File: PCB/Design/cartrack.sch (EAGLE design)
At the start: 1 part

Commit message: Done most of the GSM schematic.
Power and GPS remain
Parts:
- added C1: 1uF, resistor:C-EUC0603
- added LED1: (no value), led:LEDSML0603
- added Q1, Q2: (no value), semicon-smd-ipc:NPN-TRANSISTOR_SOT23W
- added R1, R2, R3: 22R, resistor:R-EU_R0603
- added R4, R5, R6, R7: 4k7, resistor:R-EU_R0603
- added R8: 300, resistor:R-EU_R0603
- added U$3: SIMHOLDER, SparkFun-Connectors:SIMHOLDER
- added U$4: SMF05C, Simplex-DiscreteSemi:SMF05C
- added U1: ATMEGA644P-20AU, Atmel_By_element14_Batch_1:ATMEGA644P-20AU
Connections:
- new net +2V8: U$1.VDD_EXT, U1.AVCC, U1.VCC, U1.VCC_2, U1.VCC_3
- new net +4V: LED1.A, U$1.VBAT1, U$1.VBAT2, U$1.VBAT3
- new net 0V: C1.2, R5.1, R7.1, U$1.AGND, U$1.GND1, U$1.GND2, U$1.GND3, U$1.GND4, U$1.GND5, U$1.GND6, U$1.GND7, U$1.GND8, U$3.C5, U$4.ANODE, U1.GND, U1.GND_2, U1.GND_3, U1.GND_4
- new net GSM_PWR: Q1.C, U$1.PWRKEY
- new net GSM_RX: U$1.RXD, U1.PD3
- new net GSM_STATUS: U$1.STATUS, U1.PD5
- new net GSM_TX: U$1.TXD, U1.PD2
- new net N$1: R1.1, U$3.C7, U$4.CATODE1
- new net N$10: LED1.C, R8.2
- new net N$2: R2.2, U$3.C3, U$4.CATODE5
- new net N$3: R3.2, U$3.C2, U$4.CATODE3
- new net N$4: Q1.E, R5.2
- new net N$5: Q1.B, R4.2
- new net N$6: R4.1, U1.PD4
- new net N$7: Q2.E, R7.2
- new net N$8: Q2.B, R6.2
- new net N$9: Q2.C, R8.1
- new net NETLIGHT: R6.1, U$1.NETLIGHT
- new net SIM_CLK: R2.1, U$1.SIM_CLK
- new net SIM_DATA: R1.2, U$1.SIM_DATA
- new net SIM_RST: R3.1, U$1.SIM_RST
- new net SIM_VDD: C1.1, U$1.SIM_VDD, U$3.C1, U$4.CATODE2

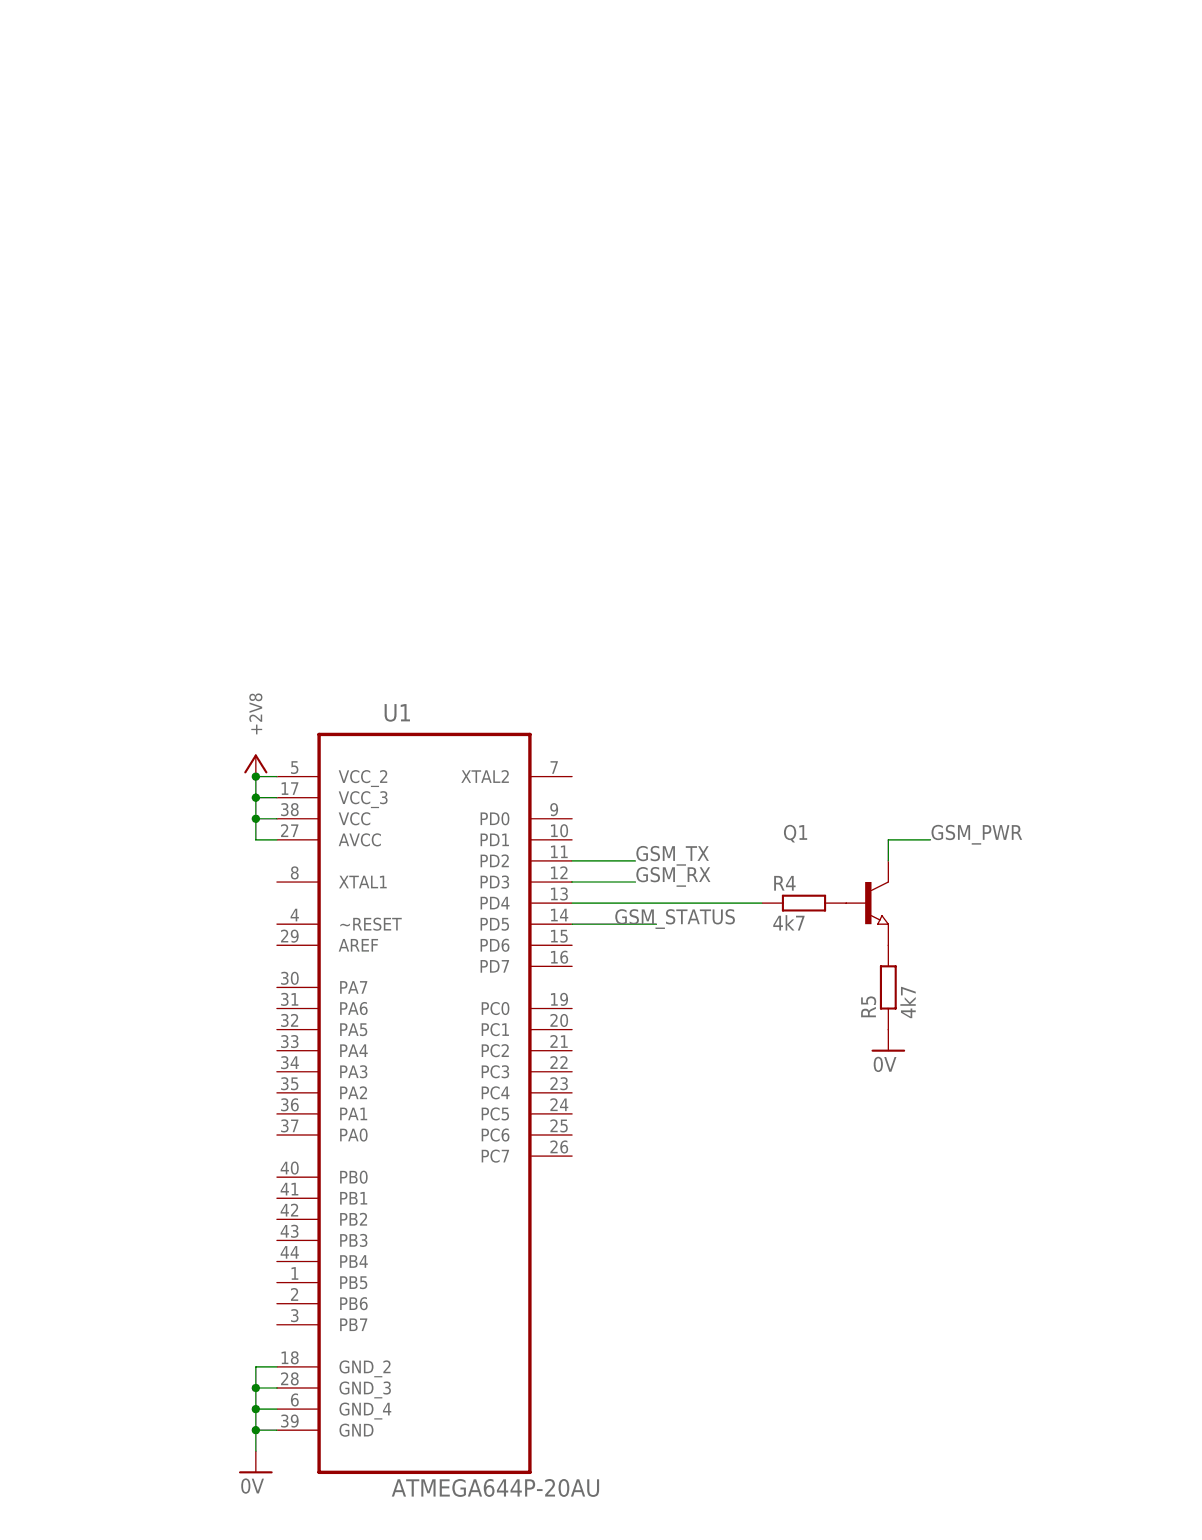
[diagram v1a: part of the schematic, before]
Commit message: Added GPS to schematic. Need to do power
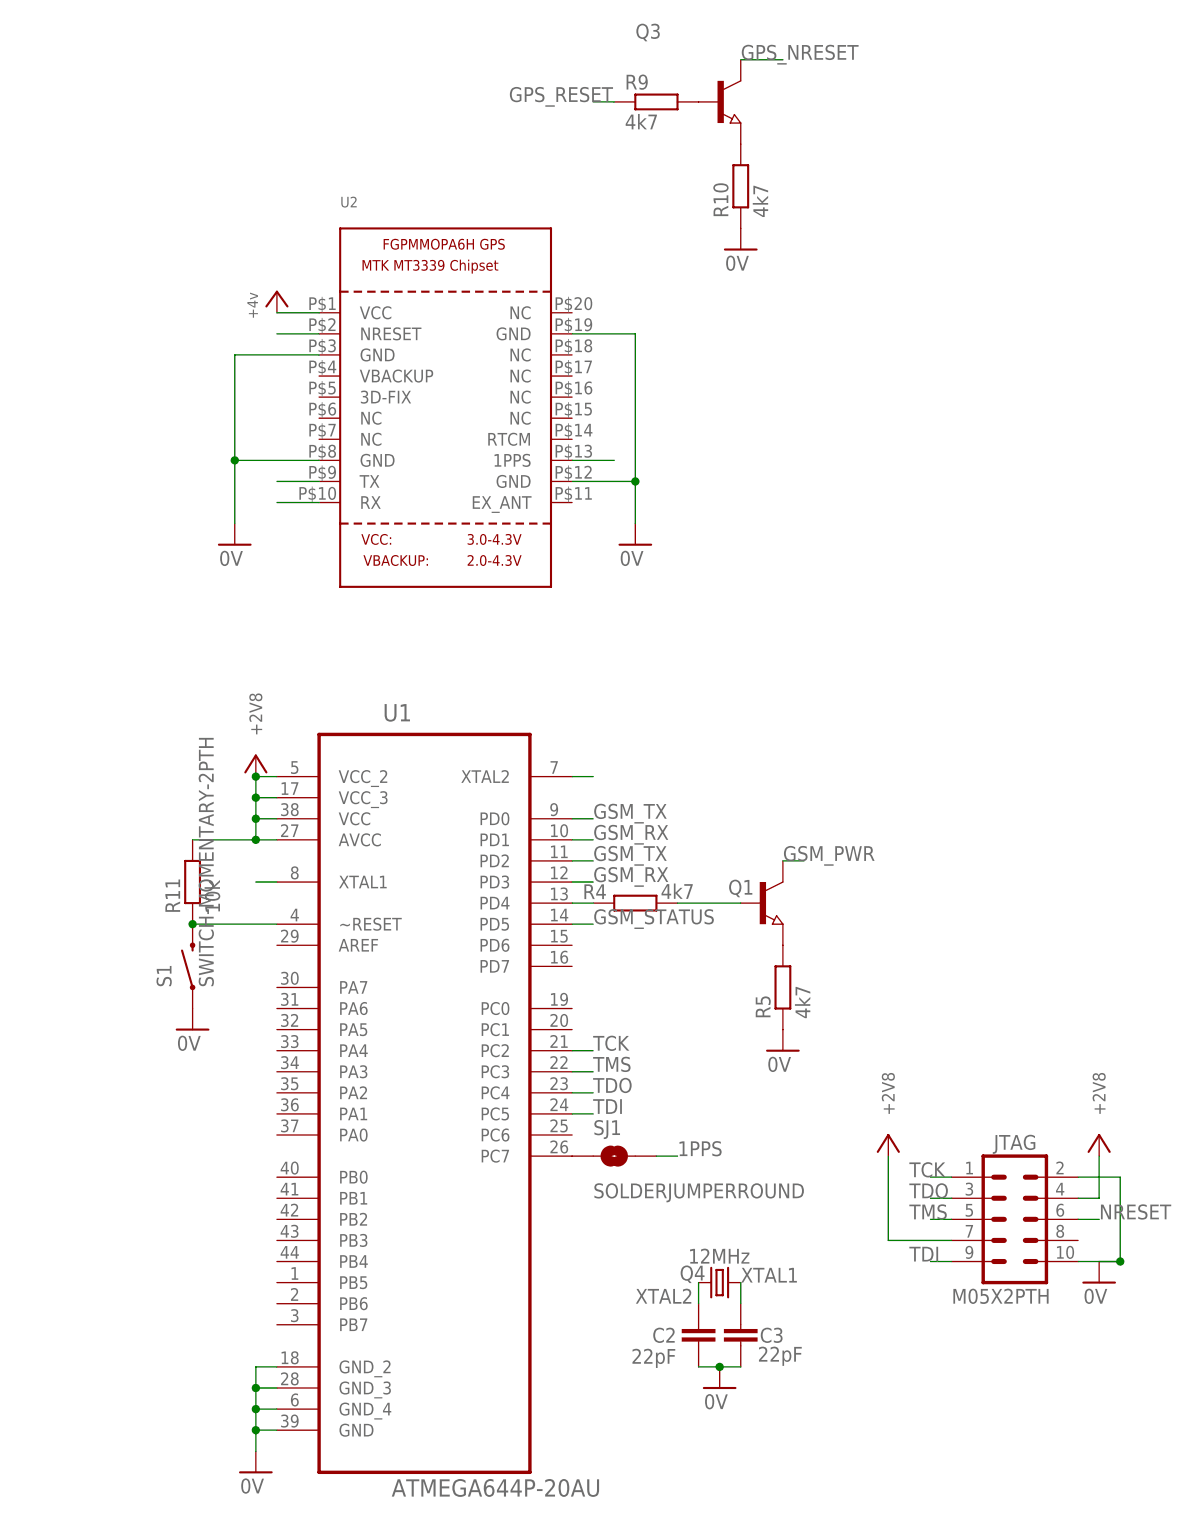
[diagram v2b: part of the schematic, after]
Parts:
- added C2, C3: 22pF, SparkFun-Passives:CAP0603-CAP
- added JTAG: M05X2PTH, SparkFun-Connectors:M05X2PTH
- added Q3: (no value), semicon-smd-ipc:NPN-TRANSISTOR_SOT23W
- added Q4: 12MHz, crystal:CRYSTALSM49
- added R10, R9: 4k7, resistor:R-EU_R0603
- added R11: 10k, resistor:R-EU_R0603
- added S1: SWITCH-MOMENTARY-2PTH, SparkFun-Electromechanical:SWITCH-MOMENTARY-2PTH
- added SJ1: SOLDERJUMPERROUND, SparkFun-Retired:SOLDERJUMPERROUND
- added U2: (no value), adafruit:GPS_FGPMMOPA6H
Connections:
- new net 1PPS: SJ1.2, U2.1PPS
- new net GPS_NRESET: Q3.C, U2.NRESET
- new net GPS_RESET: R9.1
- new net GPS_RX: U2.RX
- new net GPS_TX: U2.TX
- new net N$11: Q3.B, R9.2
- new net N$12: Q3.E, R10.2
- new net N$13: SJ1.1, U1.PC7
- new net NRESET: JTAG.6, R11.1, S1.2, U1.~RESET
- new net TCK: JTAG.1, U1.PC2
- new net TDI: JTAG.9, U1.PC5
- new net TDO: JTAG.3, U1.PC4
- new net TMS: JTAG.5, U1.PC3
- new net XTAL1: C3.1, Q4.2, U1.XTAL1
- new net XTAL2: C2.1, Q4.1, U1.XTAL2
- net +2V8: now also JTAG.4, JTAG.7, R11.2
- net +4V: now also U2.VCC
- net 0V: now also C2.2, C3.2, JTAG.10, JTAG.2, R10.1, S1.1, U2.GND@1, U2.GND@2, U2.GND@3, U2.GND@4
- net GSM_RX: now also U1.PD1
- net GSM_TX: now also U1.PD0
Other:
- moved on the sheet: Q1, R4, R5

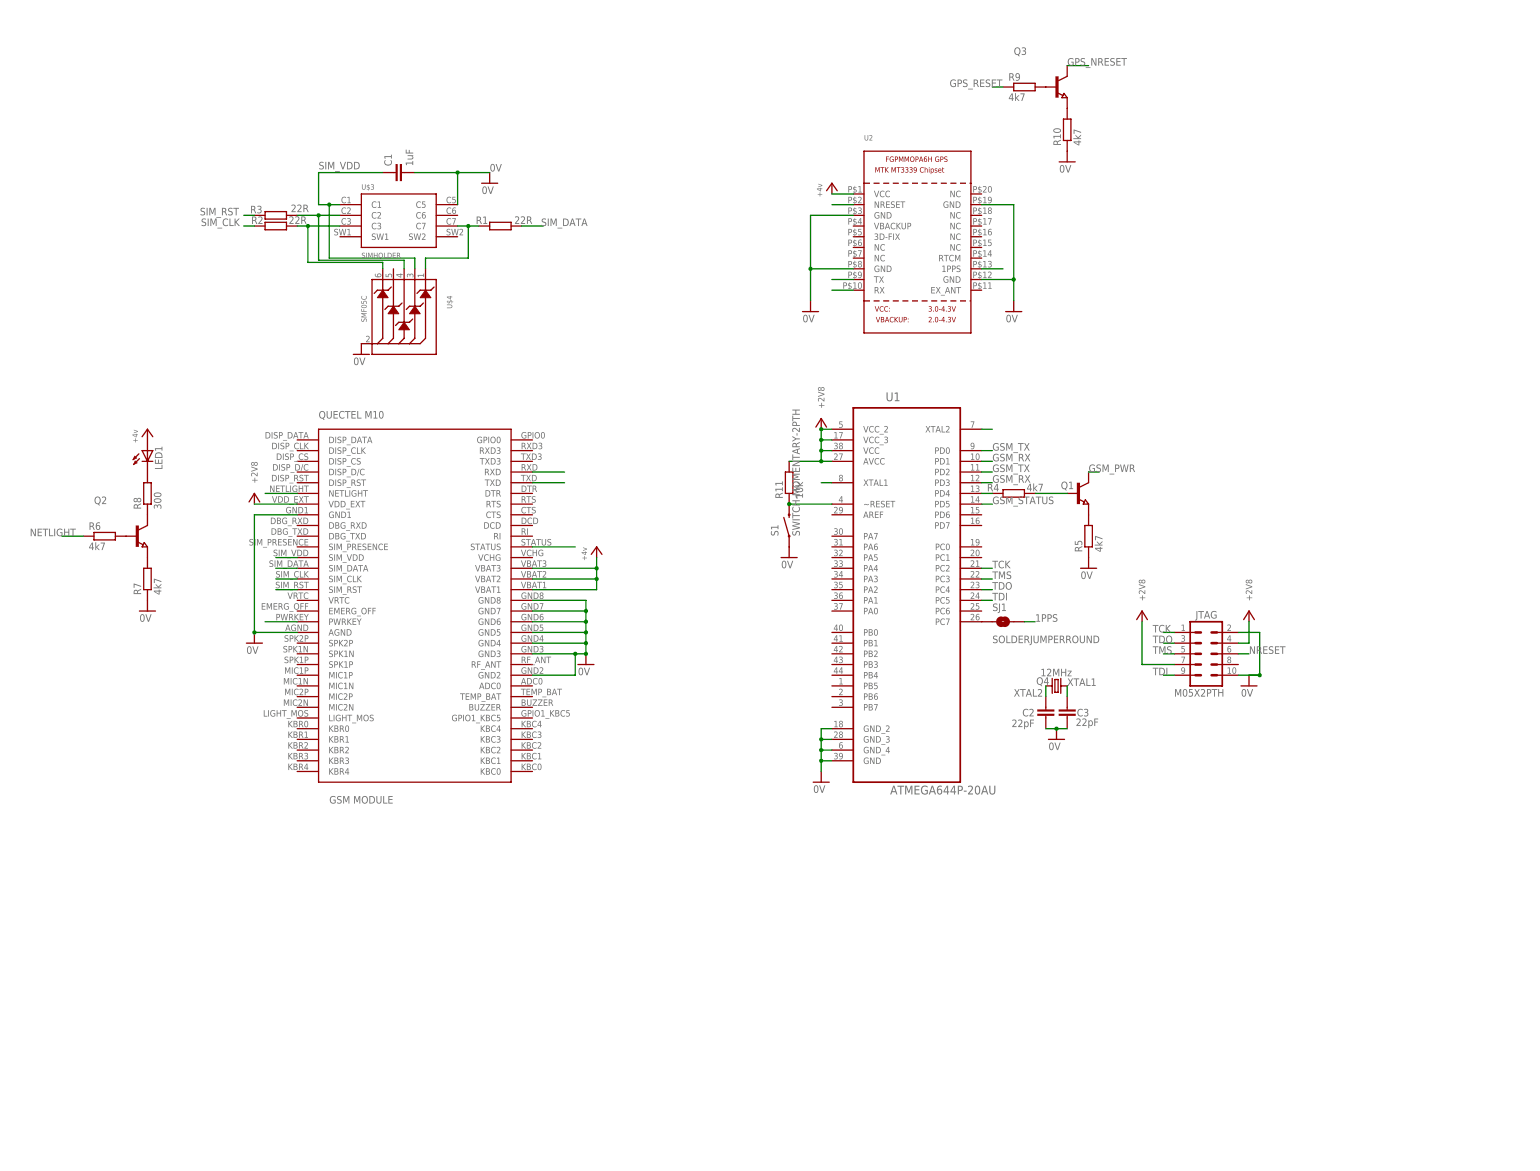
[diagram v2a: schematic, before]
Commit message: Added all major components to schematic.
Need to do the antenna, decoupling capacitors and layout
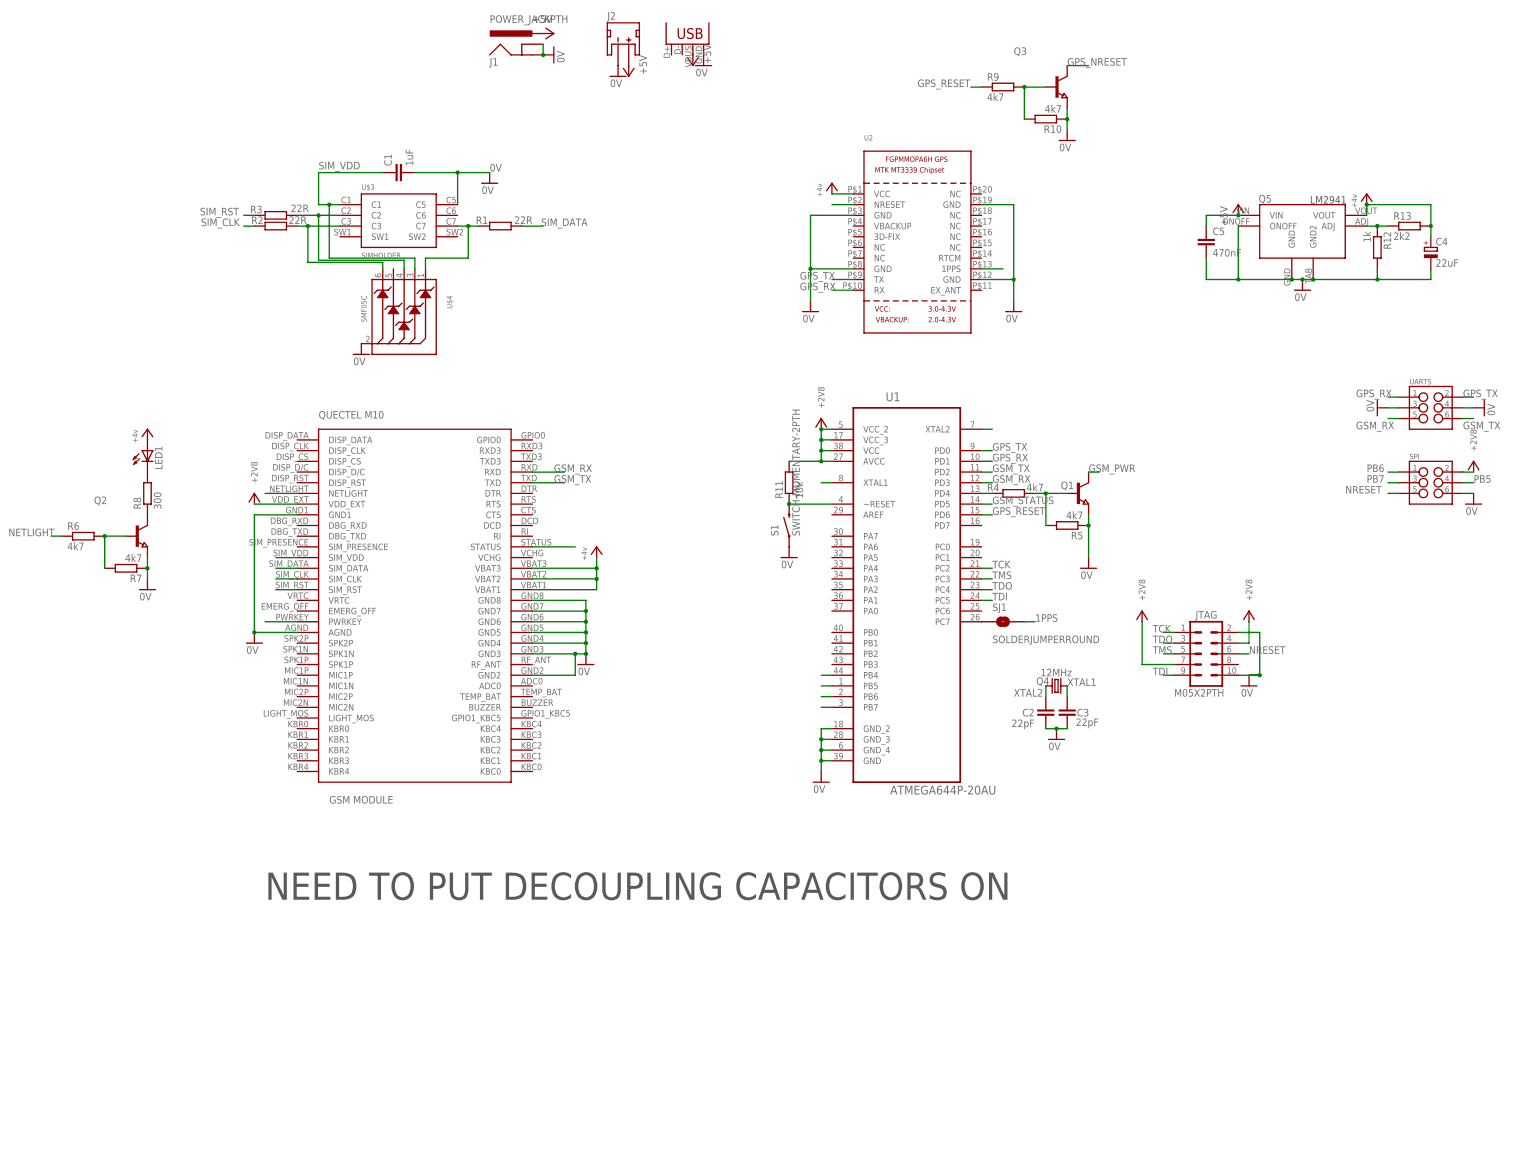
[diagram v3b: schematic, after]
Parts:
- added C4: 22uF, resistor:CPOL-EUE3.5-8
- added C5: 470nF, resistor:C-EU025-024X044
- added J1: POWER_JACKPTH, SparkFun-Connectors:POWER_JACKPTH
- added J2: (no value), SparkFun-Connectors:JST_2MM_MALE
- added JP1: USBSMD, SparkFun-Connectors:USBSMD
- added Q5: LM2941, misc:LM2941
- added R12: 1k, resistor:R-EU_R0603
- added R13: 2k2, resistor:R-EU_R0603
- added SPI, UARTS: (no value), SparkFun-Connectors:M03X2NO_SILK
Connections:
- removed net N$12: Q3.E, R10.2
- removed net N$4: Q1.E, R5.2
- new net +5V: C5.1, J1.PWR, J2.+, JP1.VBUS, Q5.VIN
- new net PB4: U1.PB4
- new net PB5: SPI.4, U1.PB5
- new net PB6: SPI.1, U1.PB6
- new net PB7: SPI.3, U1.PB7
- net +2V8: now also SPI.2
- net +4V: now also C4.+, Q5.VOUT, R13.2
- net 0V: now also C4.-, C5.2, J1.GND, J1.GNDBREAK, J2.-, JP1.GND, Q1.E, Q2.E, Q3.E, Q5.GND, Q5.GND2, Q5.ONOFF, R12.2, SPI.6, UARTS.3, UARTS.4
- net GPS_RESET: now also U1.PD6
- net GPS_RX: now also U1.PD1, UARTS.1
- net GPS_TX: now also U1.PD0, UARTS.2
- net GSM_RX: now also UARTS.5; no longer U1.PD1
- net GSM_TX: now also UARTS.6; no longer U1.PD0
- net N$11: now also R10.2
- net N$5: now also R5.2
- net N$7: now also Q5.ADJ, R12.1, R13.1; no longer Q2.E, R7.2
- net N$8: now also R7.2
- net NRESET: now also SPI.5
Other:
- note added: "NEED TO PUT DECOUPLING CAPACITORS ON"
- moved on the sheet: R10, R5, R6, R7, R9

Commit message: added to do list to schematic
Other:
- note added: "TO DO: Decoupling capacitors GSM Antenna"
- note removed: "NEED TO PUT DECOUPLING CAPACITORS ON"
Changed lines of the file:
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@@
 <sheet>
 <plain>
-<text x="12.7" y="-25.4" size="6.4516" layer="97">NEED TO PUT DECOUPLING CAPACITORS ON</text>
+<text x="20.32" y="-45.72" size="6.4516" layer="97">TO DO:
+Decoupling capacitors
+GSM Antenna</text>
 </plain>
 <instances>
@@
 </schematic>
 </drawing>
+<compatibility>
+<note version="6.3" minversion="6.2.2" severity="warning">
+Since Version 6.2.2 text objects can contain more than one line,
+which will not be processed correctly with this version.
+</note>
+</compatibility>
 </eagle>
